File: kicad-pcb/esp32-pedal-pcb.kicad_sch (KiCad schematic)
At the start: 52 parts, among them J1 USB_C_Receptacle_USB2.0_14P, SW1 SW_SPST, SW2 SW_SPST, U1 MCP73871, U2 TLV75733PDBV, U3 ESP32-S3-WROOM-1, U4 TPD2EUSB30, U6 TPS2553DBVR

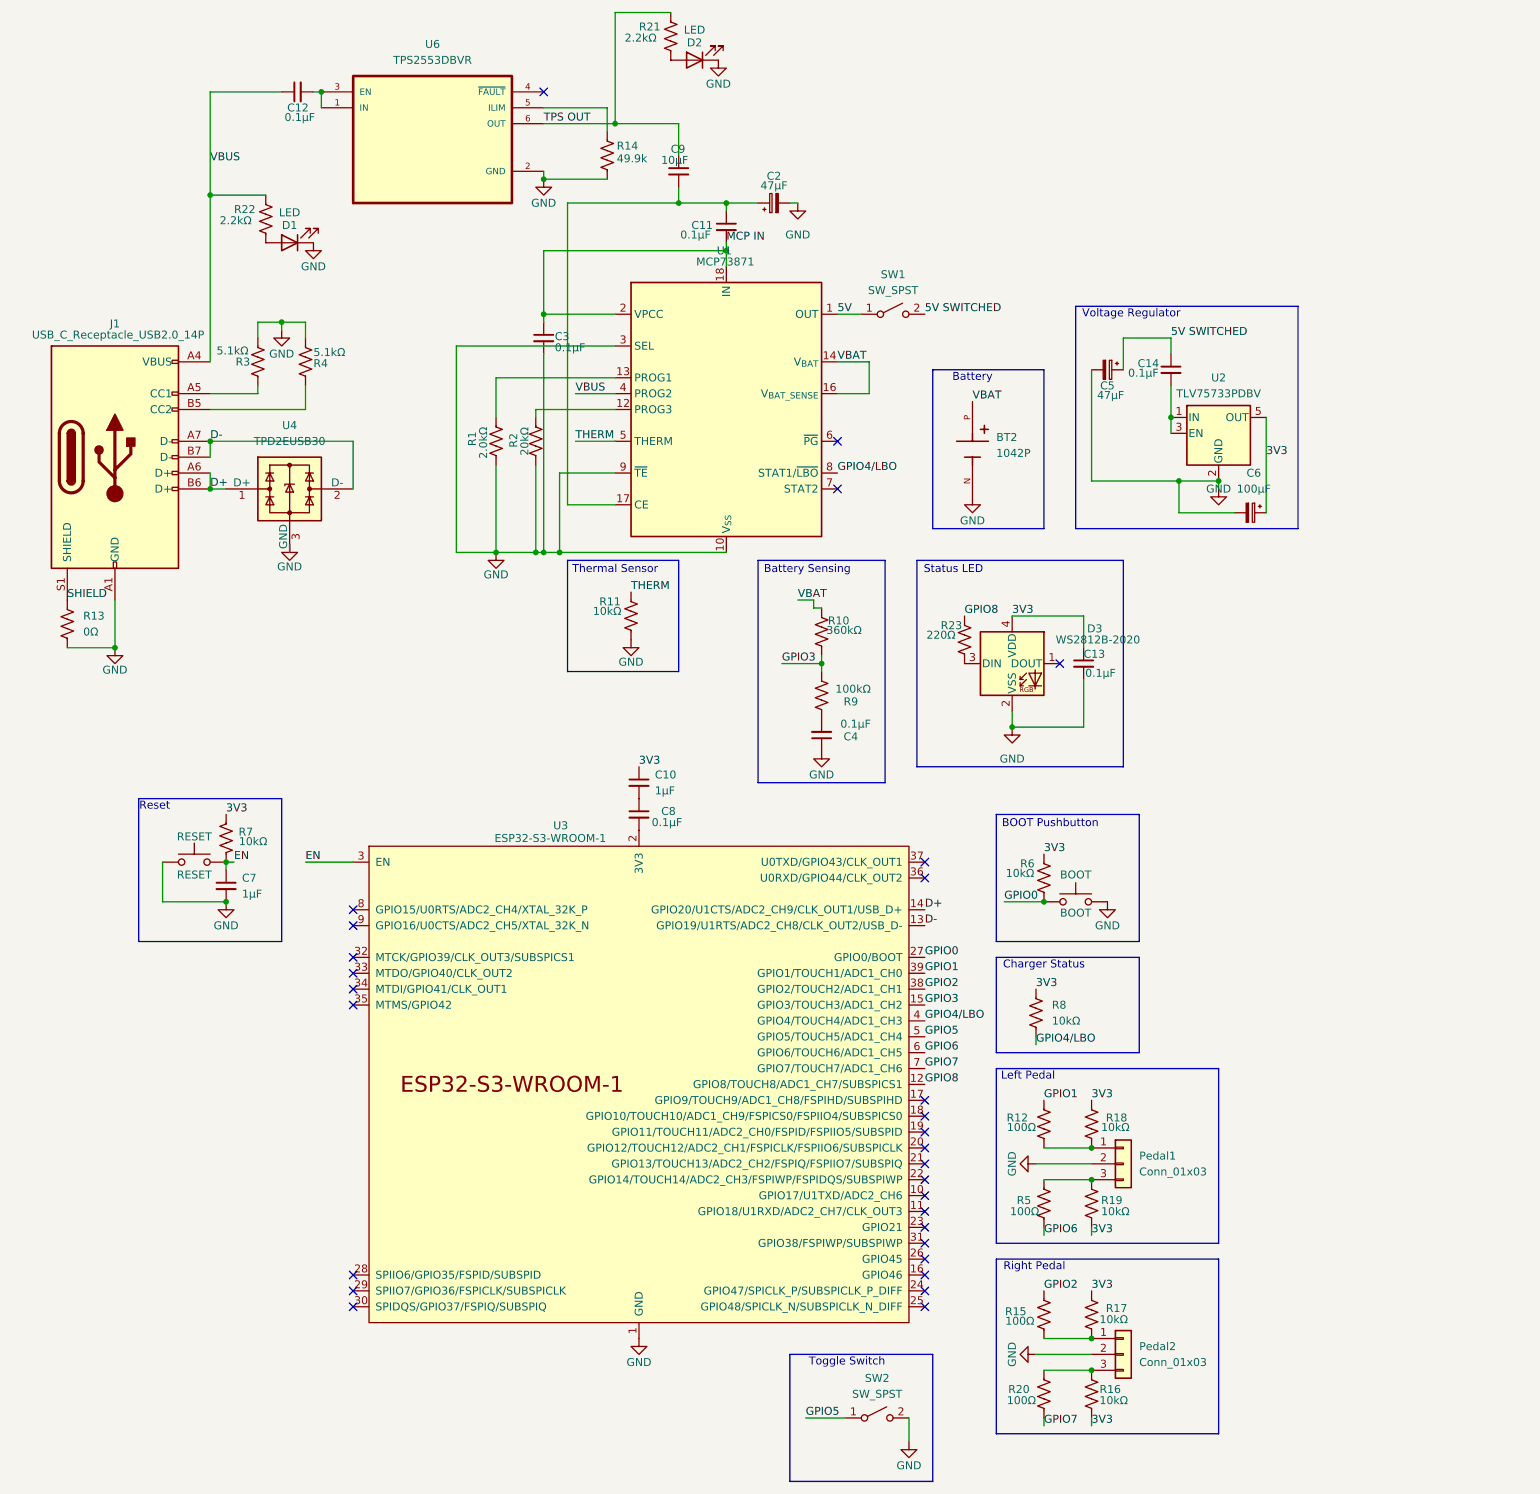
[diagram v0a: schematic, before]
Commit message: Fix watchdog timeouts and stabilize interrupt handling
- Simplified interrupt handling: removed interrupt detachment/reattachment
- Reduced debounce time from 200ms to 50ms for better responsiveness
- Removed excessive yield() calls that were causing instability
- Fixed panic issues when pedal is held down
- Fixed panic issues when pedal is not paired
- Fixed activity timer reset when pedal is pressed
- Improved ESP-NOW send reliability with proper peer management
- Cleaned up code and removed debug heartbeat messages
- Restored 5-minute inactivity timeout for deep sleep
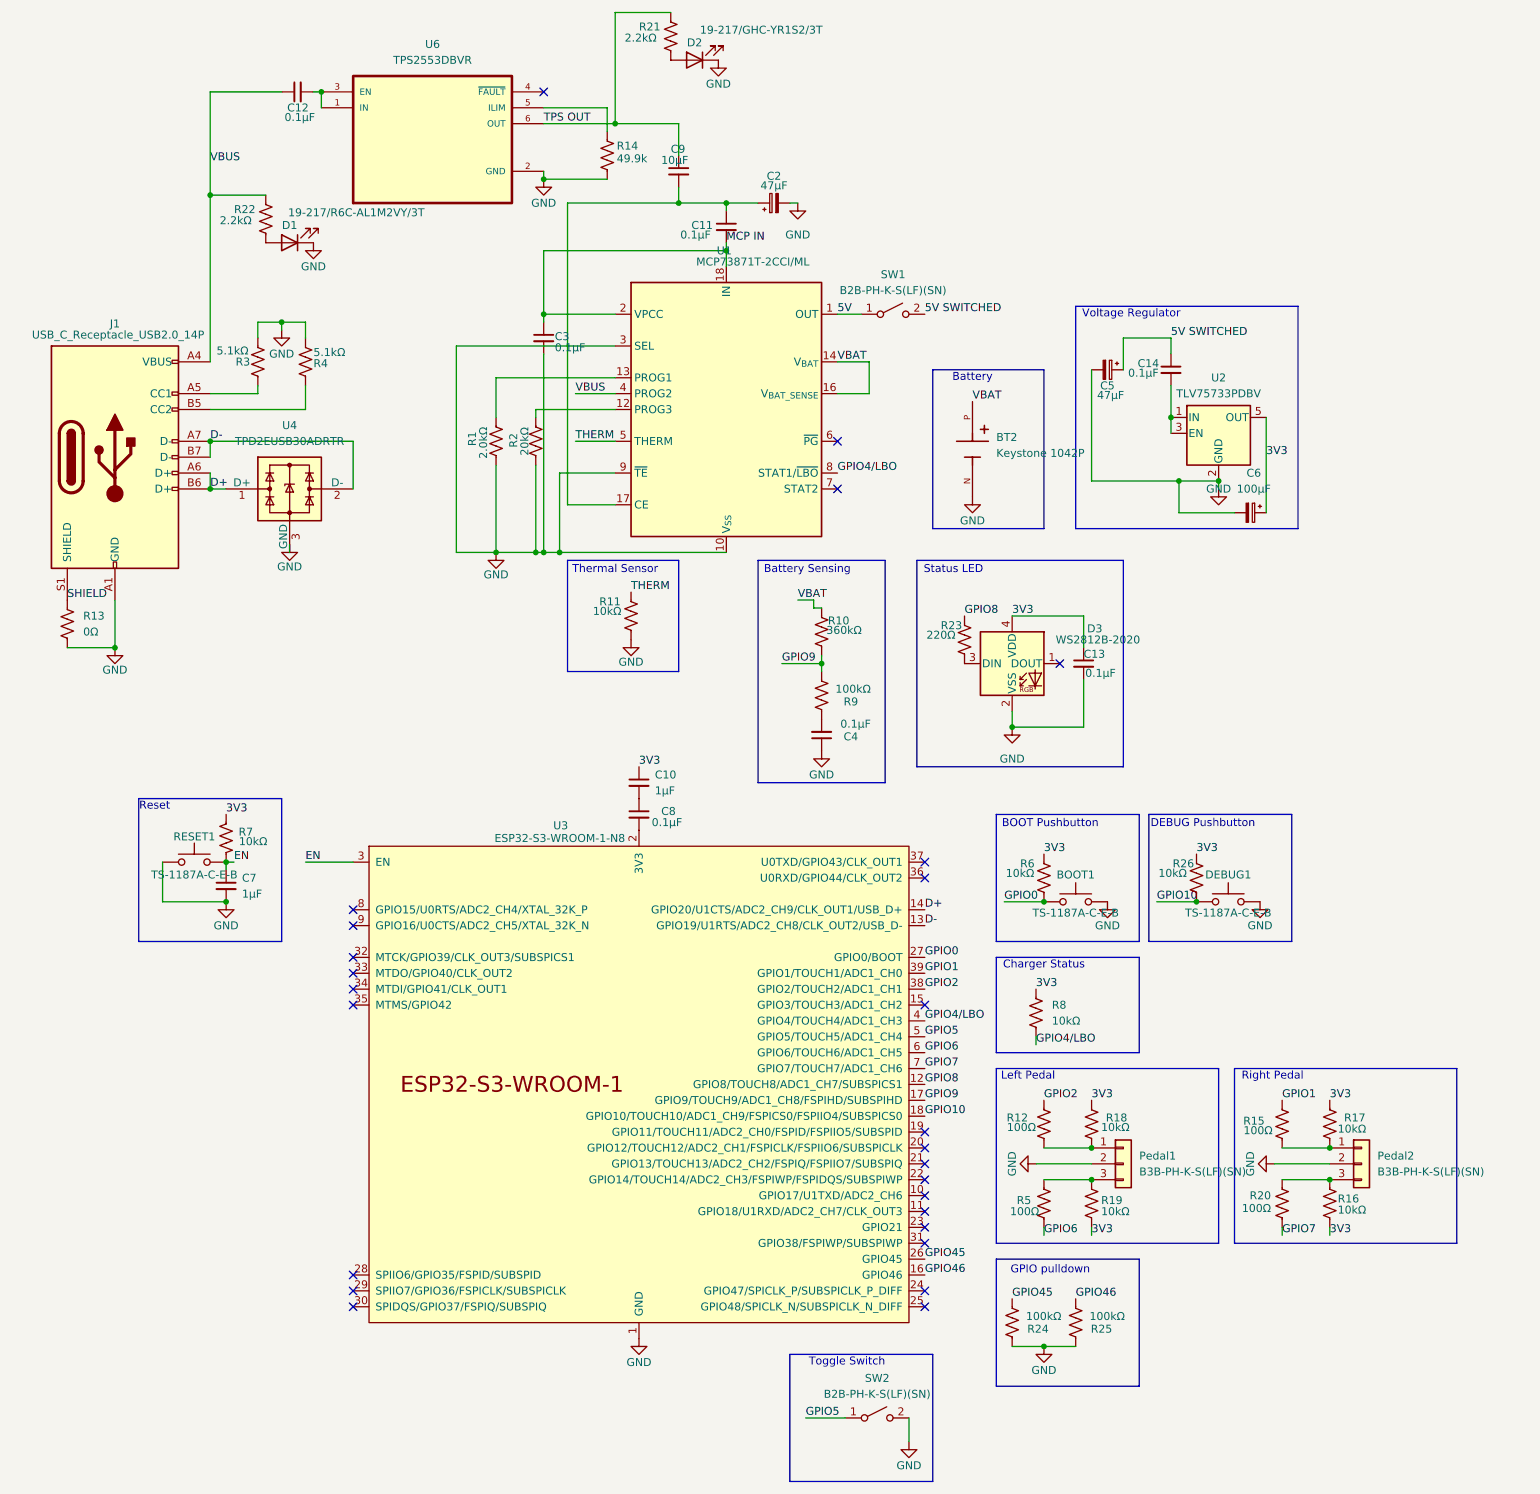
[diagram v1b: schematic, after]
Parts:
- added DEBUG1: TS-1187A-C-E-B, Button_Switch_SMD:SW_Push_1P1T_XKB_TS-1187A, symbol Switch:SW_Push
- added R24, R25: 100kΩ, Resistor_SMD:R_0603_1608Metric, symbol Device:R_US
- added R26: 10kΩ, Resistor_SMD:R_0603_1608Metric, symbol Device:R_US
- BOOT1: renamed from BOOT; value BOOT -> TS-1187A-C-E-B
- BT2: value 1042P -> Keystone 1042P
- D1: value LED -> 19-217/R6C-AL1M2VY/3T
- D2: value LED -> 19-217/GHC-YR1S2/3T
- Pedal1, Pedal2: value Conn_01x03 -> B3B-PH-K-S(LF)(SN)
- RESET1: renamed from RESET; value RESET -> TS-1187A-C-E-B
- SW1, SW2: value SW_SPST -> B2B-PH-K-S(LF)(SN)
- U1: value MCP73871 -> MCP73871T-2CCI/ML
- U3: value ESP32-S3-WROOM-1 -> ESP32-S3-WROOM-1-N8
- U4: value TPD2EUSB30 -> TPD2EUSB30ADRTR
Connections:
- net 3V3: now also R26.1
- net GND: now also DEBUG1.2, R24.1, R25.1
- net GPIO1: now also R15.2; no longer R12.2
- net GPIO2: now also R12.2; no longer R15.2
- net GPIO46: now reaches U3.16 (GPIO46)
- net GPIO46: now also R25.2
- net GPIO9: now reaches U3.17 (GPIO9/TOUCH9/ADC1_CH8/FSPIHD/SUBSPIHD)
- net GPIO9: now also R10.2, R9.2
- net GPIO10: now reaches U3.18 (GPIO10/TOUCH10/ADC1_CH9/FSPICS0/FSPIIO4/SUBSPICS0)
- net GPIO10: now also DEBUG1.1, R26.2
- net GPIO45: now reaches U3.26 (GPIO45)
- net GPIO45: now also R24.2
- removed net GPIO3: R10.2, R9.2, U3.15 (GPIO3/TOUCH3/ADC1_CH2)
- no-connect marks 29 -> 26
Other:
- note added: "DEBUG Pushbutton"
- note added: "GPIO pulldown"
- moved on the sheet: Pedal2, R15, R16, R17, R20

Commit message: Update board docs images and KiCad sources
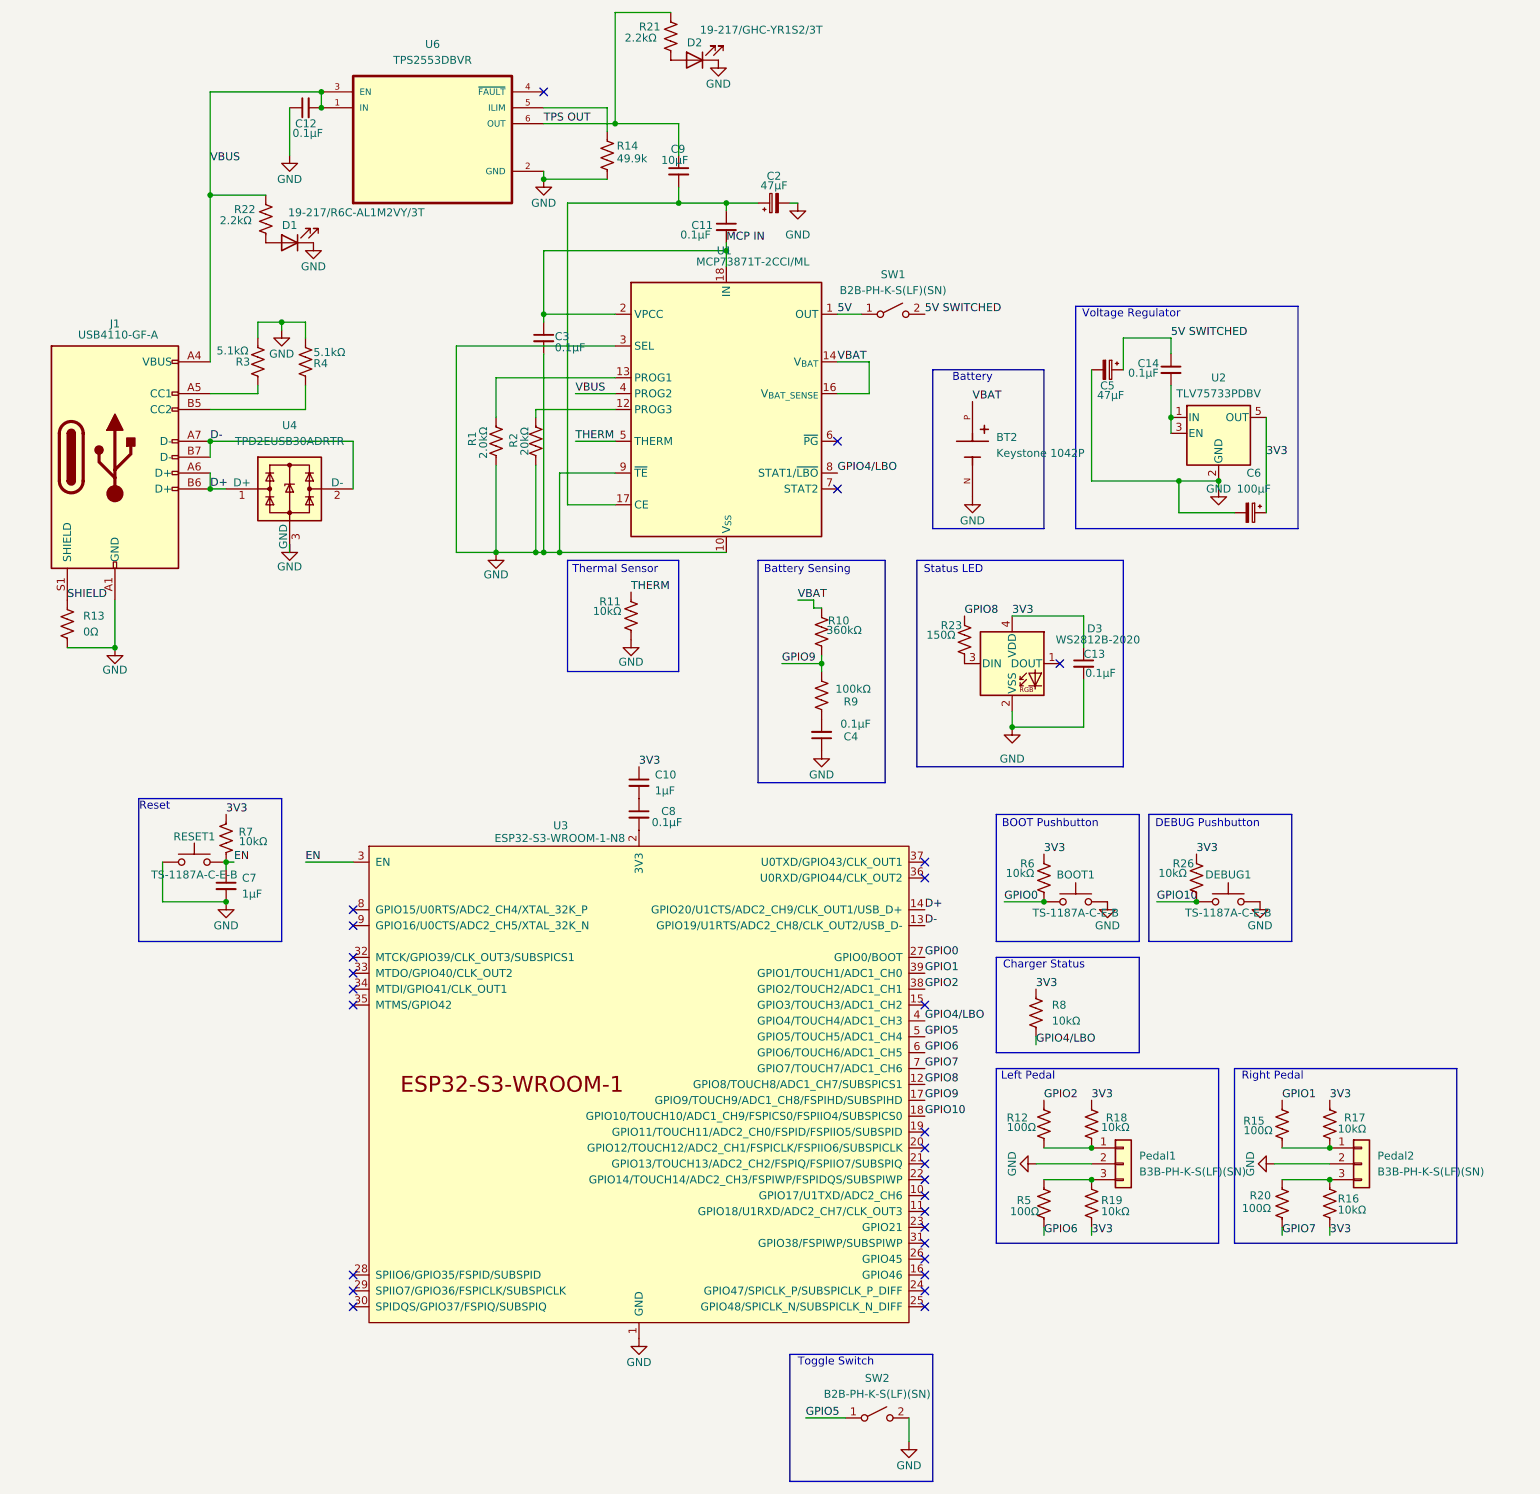
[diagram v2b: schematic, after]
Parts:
- removed R24, R25: 100kΩ, Resistor_SMD:R_0603_1608Metric, symbol Device:R_US
- J1: value USB_C_Receptacle_USB2.0_14P -> USB4110-GF-A
- R23: value 220Ω -> 150Ω
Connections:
- net GND: now also C12.1
- net VBUS: now also C12.2, U6.1 (IN), U6.3 (EN); no longer C12.1
- net GPIO45: no longer names the net of U3.26 (GPIO45)
- net GPIO46: no longer names the net of U3.16 (GPIO46)
- no-connect marks 26 -> 28
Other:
- note removed: "GPIO pulldown"
- moved on the sheet: C12
